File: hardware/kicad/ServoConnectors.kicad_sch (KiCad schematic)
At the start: 3 parts

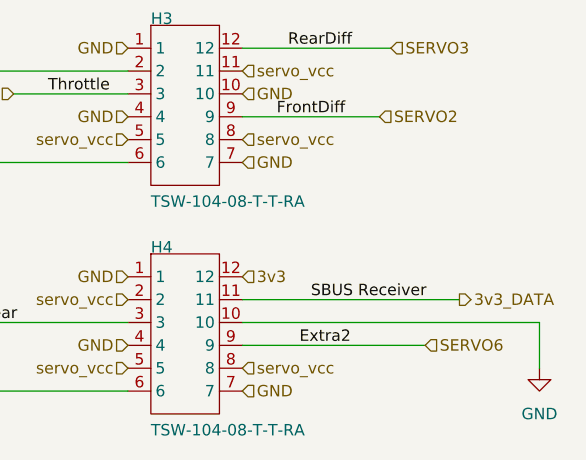
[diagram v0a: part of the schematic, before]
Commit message: servo buck and diode done, about to change order so highest current servos are closer to buck output
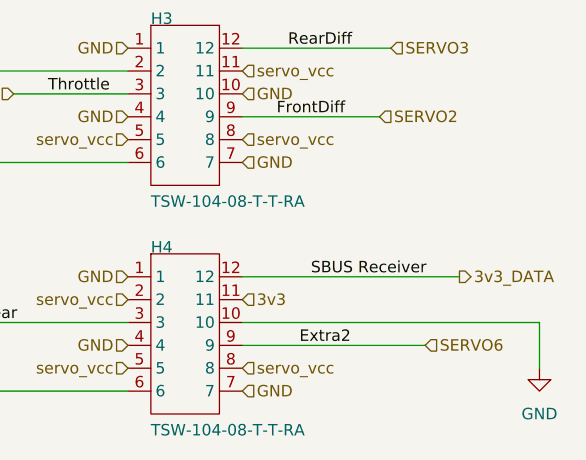
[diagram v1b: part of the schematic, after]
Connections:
- net 3v3: now also H4.11; no longer H4.12
- net 3v3_DATA: now also H4.12; no longer H4.11
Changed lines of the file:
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@@
-	(wire
-		(pts
-			(xy 187.96 106.68) (xy 163.83 106.68)
-		)
-		(stroke
-			(width 0)
-			(type default)
-		)
-	)
 	(wire
 		(pts
@@
 		(pts
 			(xy 196.85 109.22) (xy 196.85 114.3)
+		)
+		(stroke
+			(width 0)
+			(type default)
+		)
+	)
+	(wire
+		(pts
+			(xy 187.96 104.14) (xy 163.83 104.14)
 		)
 		(stroke
@@
 		)
 	)
+	(label "SBUS Receiver"
+		(at 171.45 104.14 0)
+		(effects
+			(font
+				(size 1.27 1.27)
+			)
+			(justify left bottom)
+		)
+	)
 	(label "RearDiff"
 		(at 168.91 78.74 0)
@@
 		)
 	)
-	(label "SBUS Receiver"
-		(at 171.45 106.68 0)
-		(effects
-			(font
-				(size 1.27 1.27)
-			)
-			(justify left bottom)
-		)
-	)
 	(hierarchical_label "THROTTLE_DATA_(SERVO_0)"
 		(shape input)
@@
 			)
 			(justify left)
-		)
-	)
-	(hierarchical_label "SERVO1"
-		(shape input)
-		(at 127 91.44 180)
-		(effects
-			(font
-				(size 1.27 1.27)
-			)
-			(justify right)
-		)
-	)
-	(hierarchical_label "GND"
-		(shape input)
-		(at 151.13 86.36 180)
-		(effects
-			(font
-				(size 1.27 1.27)
-			)
-			(justify right)
-		)
-	)
-	(hierarchical_label "GND"
-		(shape input)
-		(at 163.83 116.84 0)
-		(effects
-			(font
-				(size 1.27 1.27)
-			)
-			(justify left)
-		)
-	)
-	(hierarchical_label "servo_vcc"
-		(shape input)
-		(at 151.13 88.9 180)
-		(effects
-			(font
-				(size 1.27 1.27)
-			)
-			(justify right)
 		)
 	)
 	(hierarchical_label "3v3_DATA"
 		(shape output)
-		(at 187.96 106.68 0)
+		(at 187.96 104.14 0)
+		(effects
+			(font
+				(size 1.27 1.27)
+			)
+			(justify left)
+		)
+	)
+	(hierarchical_label "SERVO1"
+		(shape input)
+		(at 127 91.44 180)
+		(effects
+			(font
+				(size 1.27 1.27)
+			)
+			(justify right)
+		)
+	)
+	(hierarchical_label "GND"
+		(shape input)
+		(at 151.13 86.36 180)
+		(effects
+			(font
+				(size 1.27 1.27)
+			)
+			(justify right)
+		)
+	)
+	(hierarchical_label "GND"
+		(shape input)
+		(at 163.83 116.84 0)
+		(effects
+			(font
+				(size 1.27 1.27)
+			)
+			(justify left)
+		)
+	)
+	(hierarchical_label "servo_vcc"
+		(shape input)
+		(at 151.13 88.9 180)
+		(effects
+			(font
+				(size 1.27 1.27)
+			)
+			(justify right)
+		)
+	)
+	(hierarchical_label "3v3"
+		(shape input)
+		(at 163.83 106.68 0)
 		(effects
 			(font
@@
 		)
 	)
-	(hierarchical_label "3v3"
-		(shape input)
-		(at 163.83 104.14 0)
-		(effects
-			(font
-				(size 1.27 1.27)
-			)
-			(justify left)
-		)
-	)

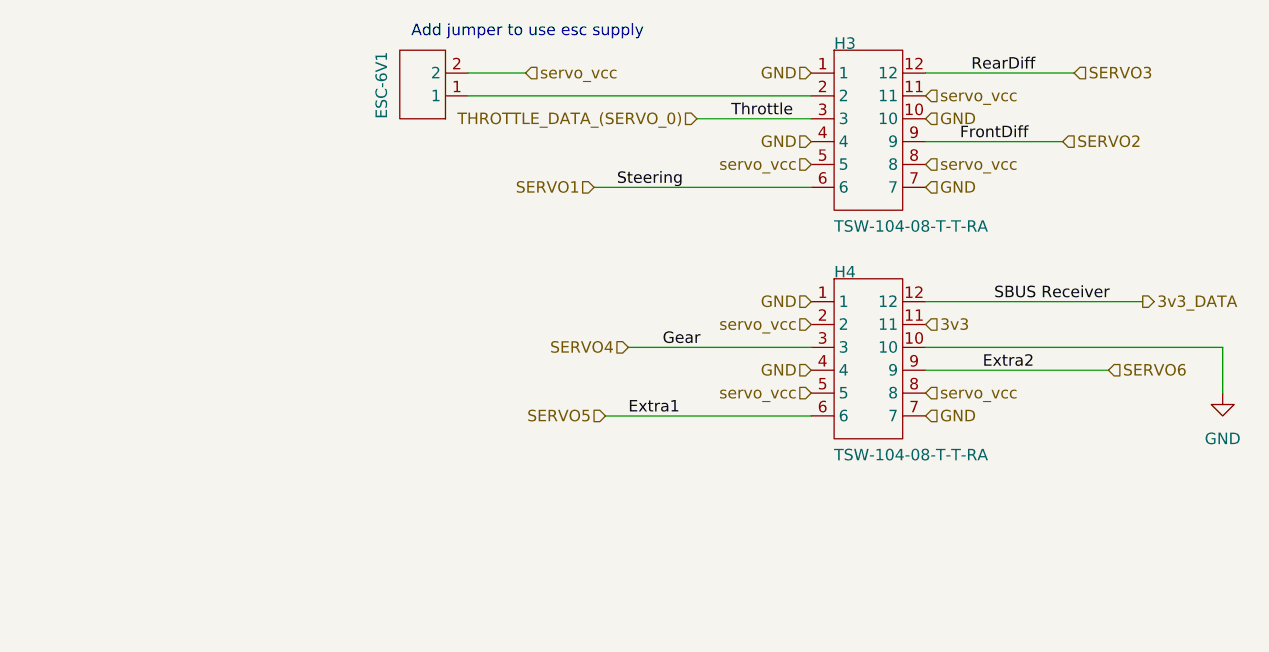
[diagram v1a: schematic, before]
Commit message: servo current sensor also done
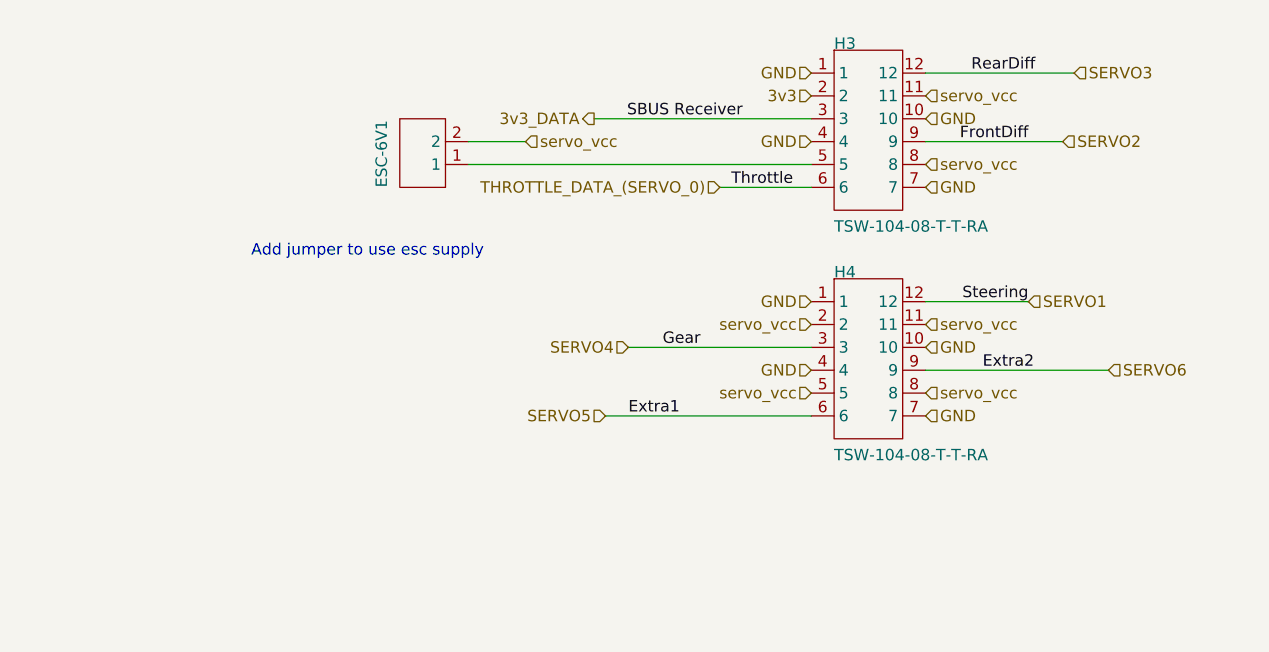
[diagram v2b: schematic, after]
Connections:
- net 3v3: now also H3.2; no longer H4.11
- net 3v3_DATA: now also H3.3; no longer H4.12
- net SERVO1: now also H4.12; no longer H3.6
- net THROTTLE_DATA_(SERVO_0): now also H3.6; no longer H3.3
- net servo_vcc: now also H4.11; no longer H3.5
- net at ESC-6V1.1: now also H3.5; no longer H3.2
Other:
- moved on the sheet: ESC-6V1

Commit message: new led connector
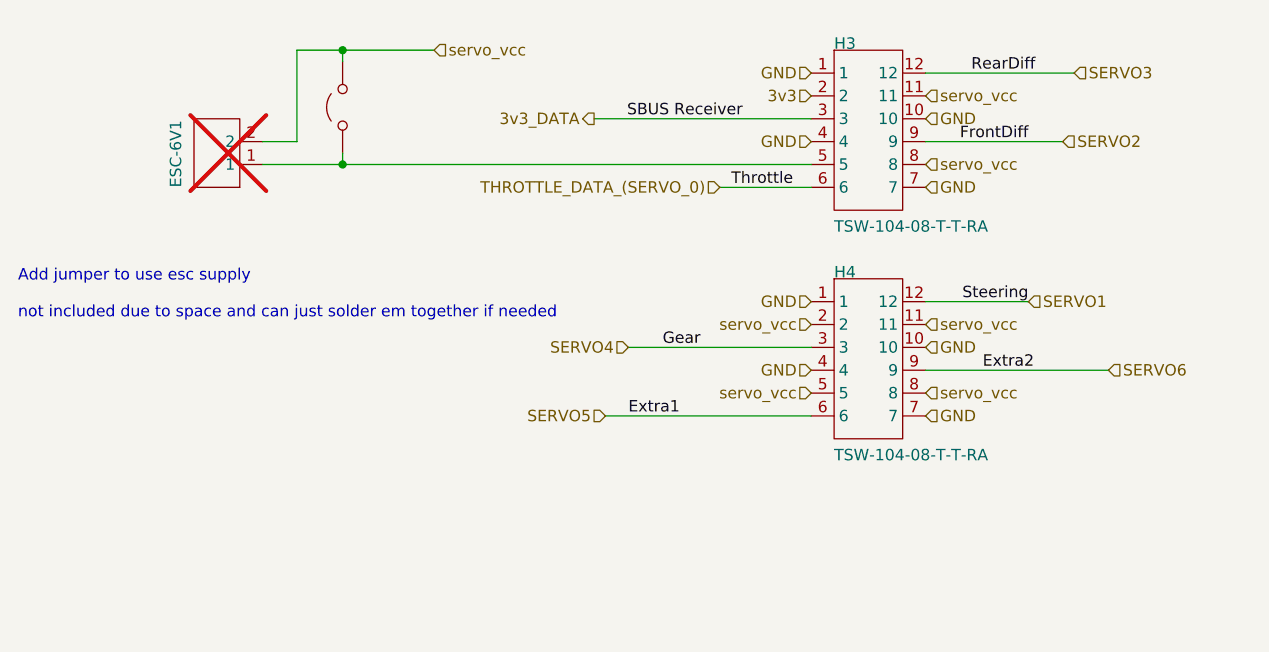
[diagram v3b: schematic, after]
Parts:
- added JP2101: Jumper_2_Open, PCM_SparkFun-Jumper:Jumper_2_NO, symbol Jumper:Jumper_2_Open
- ESC-6V1: now not fitted; now left out of the parts list
- H3: port11 (none) -> Rdiff; port2 (none) -> sbus; port5 (none) -> throttle; port8 (none) -> Fdiff
- H4: port11 (none) -> steer; port2 (none) -> gear; port5 (none) -> xtr1; port8 (none) -> xtr2
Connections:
- net servo_vcc: now also JP2101.2 (B)
- net at ESC-6V1.1, H3.5: now also JP2101.1 (A)
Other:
- note added: "Add jumper to use esc supply not included due to space and can just solder em together if needed"
- note removed: "Add jumper to use esc supply"
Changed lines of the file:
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@@
 	(generator_version "9.0")
 	(paper "A4")
-	(text "Add jumper to use esc supply"
+	(text "Add jumper to use esc supply\n\nnot included due to space and can just solder em together if needed"
 		(exclude_from_sim no)
-		(at 88.9 99.314 0)
+		(at 62.992 106.172 0)
 		(effects
 			(font
@@
 		)
 	)
-	(wire
-		(pts
-			(xy 113.03 86.36) (xy 119.38 86.36)
+	(junction
+		(at 99.06 88.9)
+		(diameter 0)
+		(color 0 0 0 0)
+	)
+	(junction
+		(at 99.06 76.2)
+		(diameter 0)
+		(color 0 0 0 0)
+	)
+	(wire
+		(pts
+			(xy 93.98 76.2) (xy 99.06 76.2)
+		)
+		(stroke
+			(width 0)
+			(type default)
+		)
+	)
+	(wire
+		(pts
+			(xy 93.98 86.36) (xy 90.17 86.36)
+		)
+		(stroke
+			(width 0)
+			(type default)
+		)
+	)
+	(wire
+		(pts
+			(xy 99.06 88.9) (xy 151.13 88.9)
 		)
 		(stroke
@@
 	(wire
 		(pts
+			(xy 99.06 87.63) (xy 99.06 88.9)
+		)
+		(stroke
+			(width 0)
+			(type default)
+		)
+	)
+	(wire
+		(pts
+			(xy 99.06 76.2) (xy 109.22 76.2)
+		)
+		(stroke
+			(width 0)
+			(type default)
+		)
+	)
+	(wire
+		(pts
 			(xy 180.34 78.74) (xy 163.83 78.74)
 		)
@@
 	(wire
 		(pts
-			(xy 113.03 88.9) (xy 151.13 88.9)
+			(xy 90.17 88.9) (xy 99.06 88.9)
 		)
 		(stroke
@@
 	(wire
 		(pts
+			(xy 99.06 76.2) (xy 99.06 77.47)
+		)
+		(stroke
+			(width 0)
+			(type default)
+		)
+	)
+	(wire
+		(pts
 			(xy 179.07 86.36) (xy 163.83 86.36)
+		)
+		(stroke
+			(width 0)
+			(type default)
+		)
+	)
+	(wire
+		(pts
+			(xy 93.98 76.2) (xy 93.98 86.36)
 		)
 		(stroke
@@
 	(hierarchical_label "servo_vcc"
 		(shape input)
-		(at 119.38 86.36 0)
+		(at 109.22 76.2 0)
 		(effects
 			(font
@@
 			)
 			(justify left)
+		)
+	)
+	(symbol
+		(lib_id "Jumper:Jumper_2_Open")
+		(at 99.06 82.55 90)
+		(unit 1)
+		(exclude_from_sim no)
+		(in_bom yes)
+		(on_board yes)
+		(dnp no)
+		(fields_autoplaced yes)
+		(property "Reference" "JP2101"
+			(at 100.33 81.2799 90)
+			(effects
+				(font
+					(size 1.27 1.27)
+				)
+				(justify right)
+				(hide yes)
+			)
+		)
+		(property "Value" "Jumper_2_Open"
+			(at 100.33 83.8199 90)
+			(effects
+				(font
+					(size 1.27 1.27)
+				)
+				(justify right)
+				(hide yes)
+			)
+		)
+		(property "Footprint" "PCM_SparkFun-Jumper:Jumper_2_NO"
+			(at 99.06 82.55 0)
+			(effects
+				(font
+					(size 1.27 1.27)
+				)
+				(hide yes)
+			)
+		)
+		(property "Datasheet" "~"
+			(at 99.06 82.55 0)
+			(effects
+				(font
+					(size 1.27 1.27)
+				)
+				(hide yes)
+			)
+		)
+		(property "Description" "Jumper, 2-pole, open"
+			(at 99.06 82.55 0)
+			(effects
+				(font
+					(size 1.27 1.27)
+				)
+				(hide yes)
+			)
+		)
+		(pin "1"
+		)
+		(pin "2"
+		)
+		(instances
+			(project ""
+				(path "/3f85abf4-0b95-4c4a-b7e9-06f59ca1ea3d/5c2e021f-c2d4-49e2-8c36-9a64f1f12001/e0f45e16-4740-446f-ae55-03461fa88791"
+					(reference "JP2101")
+					(unit 1)
+				)
+			)
 		)
 	)
@@
 			)
 		)
+		(property "port2" "sbus"
+			(at 157.48 85.09 0)
+			(effects
+				(font
+					(size 1.27 1.27)
+				)
+				(hide yes)
+			)
+		)
+		(property "port5" "throttle"
+			(at 157.48 85.09 0)
+			(effects
+				(font
+					(size 1.27 1.27)
+				)
+				(hide yes)
+			)
+		)
+		(property "port8" "Fdiff"
+			(at 157.48 85.09 0)
+			(effects
+				(font
+					(size 1.27 1.27)
+				)
+				(hide yes)
+			)
+		)
+		(property "port11" "Rdiff"
+			(at 157.48 85.09 0)
+			(effects
+				(font
+					(size 1.27 1.27)
+				)
+				(hide yes)
+			)
+		)
 		(pin "1"
 		)
@@
 			)
 		)
+		(property "port2" "gear"
+			(at 157.48 110.49 0)
+			(effects
+				(font
+					(size 1.27 1.27)
+				)
+				(hide yes)
+			)
+		)
+		(property "port5" "xtr1"
+			(at 157.48 110.49 0)
+			(effects
+				(font
+					(size 1.27 1.27)
+				)
+				(hide yes)
+			)
+		)
+		(property "port8" "xtr2"
+			(at 157.48 110.49 0)
+			(effects
+				(font
+					(size 1.27 1.27)
+				)
+				(hide yes)
+			)
+		)
+		(property "port11" "steer"
+			(at 157.48 110.49 0)
+			(effects
+				(font
+					(size 1.27 1.27)
+				)
+				(hide yes)
+			)
+		)
 		(pin "4"
 		)
@@
 	(symbol
 		(lib_id "5v rail sm-easyedapro:PZ254V-11-02P")
-		(at 107.95 87.63 180)
+		(at 85.09 87.63 180)
 		(unit 1)
 		(exclude_from_sim no)
-		(in_bom yes)
-		(on_board yes)
-		(dnp no)
+		(in_bom no)
+		(on_board no)
+		(dnp yes)
 		(property "Reference" "ESC-6V1"
-			(at 104.14 91.44 90)
+			(at 81.28 91.44 90)
 			(effects
 				(font
@@
 		)
 		(property "Value" "PZ254V-11-02P"
-			(at 105.41 93.98 0)
+			(at 82.55 93.98 0)
 			(effects
 				(font
@@
 		)
 		(property "Footprint" "Connector_PinHeader_2.54mm:PinHeader_1x02_P2.54mm_Vertical"
-			(at 107.95 87.63 0)
+			(at 85.09 87.63 0)
 			(effects
 				(font
@@
 		)
 		(property "Datasheet" "https://item.szlcsc.com/datasheet/PZ254V-11-02P/502957.html"
-			(at 107.95 87.63 0)
+			(at 85.09 87.63 0)
 			(effects
 				(font
@@
 		)
 		(property "Description" "Pin Structure:1x2P Pitch:2.54mm Row Spacing:- Circluar Pins/Square Pins:Pin Header Mounting Type:Through Hole Number of Rows:1 Number of Pins:2P Current Rating:- Voltage Rating (Max):- Length of Mating Pin:6mm Insulation Height:2.5mm Length of End Connect"
-			(at 107.95 87.63 0)
+			(at 85.09 87.63 0)
 			(effects
 				(font
@@
 		)
 		(property "Manufacturer Part" "PZ254V-11-02P"
-			(at 107.95 87.63 0)
+			(at 85.09 87.63 0)
 			(effects
 				(font
@@
 		)
 		(property "Manufacturer" "XFCN(兴飞)"
-			(at 107.95 87.63 0)
+			(at 85.09 87.63 0)
 			(effects
 				(font
@@
 		)
 		(property "Supplier Part" "C492401"
-			(at 107.95 87.63 0)
+			(at 85.09 87.63 0)
 			(effects
 				(font
@@
 		)
 		(property "Supplier" "LCSC"
-			(at 107.95 87.63 0)
+			(at 85.09 87.63 0)
 			(effects
 				(font
@@
 		)
 		(property "LCSC Part Name" "1x2P 间距:2.54mm 方针 直插"
-			(at 107.95 87.63 0)
-			(effects
-				(font
+			(at 85.09 87.63 0)
+			(effects
+				(font

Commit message: starting erc check
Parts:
- ESC-6V1: footprint Connector_PinHeader_2.54mm:PinHeader_1x02_P2.54mm_Vertical -> 5v rail sm-easyedapro:HDR-TH_2P-P2.54-V-M
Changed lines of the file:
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@@
 			)
 		)
-		(property "Footprint" "Connector_PinHeader_2.54mm:PinHeader_1x02_P2.54mm_Vertical"
+		(property "Footprint" "5v rail sm-easyedapro:HDR-TH_2P-P2.54-V-M"
 			(at 85.09 87.63 0)
 			(effects

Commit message: Update KiCad footprints and schematic placements
Convert and normalize multiple KiCad footprints and adjust schematic symbol placements. Upgraded EasyEDA and JLCImport footprints to modern pcbnew/footprint format (updated fp_line/pad primitives, uuids, embedded fonts/models), adjusted 3D model offsets, and expanded pad metadata. In schematics: moved EXB2HV102JV symbol position and added mirror Y, removed fields_autoplaced, set instance project path for U3201, and updated ServoConnectors port2 label to "sbus 3V". Also refreshed various PCB fp element UUIDs in svea_powerboard_rev3.kicad_pcb.
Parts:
- H3: port2 sbus -> sbus 3V
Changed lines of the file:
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@@
 			)
 		)
-		(property "port2" "sbus"
+		(property "port2" "sbus 3V"
 			(at 157.48 85.09 0)
 			(effects

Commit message: updated more footprints
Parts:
- JP2101: footprint PCM_SparkFun-Jumper:Jumper_2_NO -> Jumper:SolderJumper-2_P1.3mm_Open_TrianglePad1.0x1.5mm
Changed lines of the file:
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@@
 			)
 		)
-		(property "Footprint" "PCM_SparkFun-Jumper:Jumper_2_NO"
+		(property "Footprint" "Jumper:SolderJumper-2_P1.3mm_Open_TrianglePad1.0x1.5mm"
 			(at 99.06 82.55 0)
 			(effects

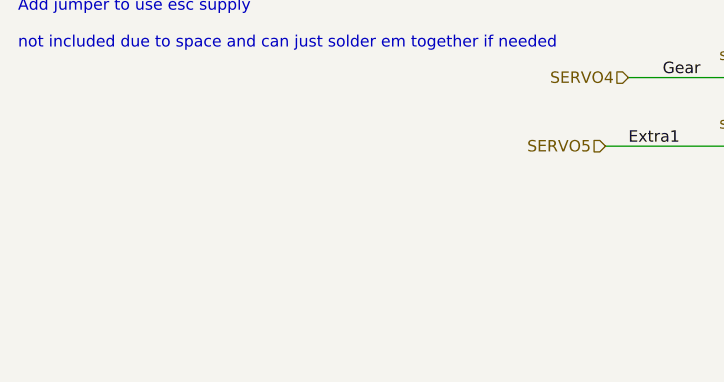
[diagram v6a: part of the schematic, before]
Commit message: starting erc check
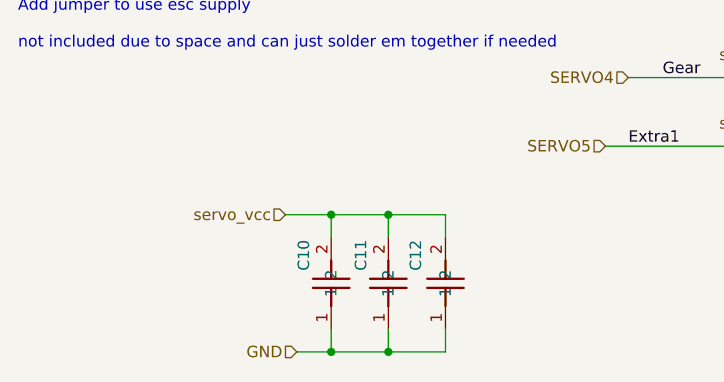
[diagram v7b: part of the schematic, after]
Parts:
- added C10, C11, C12: HGC1206R5107M100NSPJ, JLCImport:HGC1206R5107M100NSPJ, symbol JLCImport:HGC1206R5107M100NSPJ
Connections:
- net GND: now also C10.1, C11.1, C12.1
- net servo_vcc: now also C10.2, C11.2, C12.2

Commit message: update
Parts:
- added C2101: HGC1206R5107M100NSPJ, JLCImport:HGC1206R5107M100NSPJ, symbol JLCImport:HGC1206R5107M100NSPJ
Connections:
- net GND: now also C2101.1
- net servo_vcc: now also C2101.2
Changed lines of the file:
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@@
+	)
+	(junction
+		(at 110.49 139.7)
+		(diameter 0)
+		(color 0 0 0 0)
+	)
+	(junction
+		(at 110.49 124.46)
+		(diameter 0)
+		(color 0 0 0 0)
 	)
 	(junction
@@
 	)
 	(junction
+		(at 116.84 139.7)
+		(diameter 0)
+		(color 0 0 0 0)
+	)
+	(junction
+		(at 116.84 124.46)
+		(diameter 0)
+		(color 0 0 0 0)
+	)
+	(junction
 		(at 97.79 139.7)
 		(diameter 0)
@@
 	(wire
 		(pts
+			(xy 110.49 124.46) (xy 116.84 124.46)
+		)
+		(stroke
+			(width 0)
+			(type default)
+		)
+	)
+	(wire
+		(pts
 			(xy 97.79 139.7) (xy 104.14 139.7)
 		)
@@
 	(wire
 		(pts
+			(xy 110.49 139.7) (xy 116.84 139.7)
+		)
+		(stroke
+			(width 0)
+			(type default)
+		)
+	)
+	(wire
+		(pts
 			(xy 99.06 88.9) (xy 151.13 88.9)
 		)
@@
 	(wire
 		(pts
+			(xy 124.46 137.16) (xy 124.46 139.7)
+		)
+		(stroke
+			(width 0)
+			(type default)
+		)
+	)
+	(wire
+		(pts
 			(xy 184.15 111.76) (xy 163.83 111.76)
 		)
@@
 	(wire
 		(pts
-			(xy 110.49 139.7) (xy 104.14 139.7)
+			(xy 104.14 139.7) (xy 110.49 139.7)
 		)
 		(stroke
@@
 	(wire
 		(pts
+			(xy 116.84 127) (xy 116.84 124.46)
+		)
+		(stroke
+			(width 0)
+			(type default)
+		)
+	)
+	(wire
+		(pts
+			(xy 116.84 137.16) (xy 116.84 139.7)
+		)
+		(stroke
+			(width 0)
+			(type default)
+		)
+	)
+	(wire
+		(pts
 			(xy 110.49 127) (xy 110.49 124.46)
 		)
@@
 	(wire
 		(pts
+			(xy 116.84 124.46) (xy 124.46 124.46)
+		)
+		(stroke
+			(width 0)
+			(type default)
+		)
+	)
+	(wire
+		(pts
 			(xy 175.26 104.14) (xy 163.83 104.14)
 		)
@@
 	(wire
 		(pts
+			(xy 124.46 127) (xy 124.46 124.46)
+		)
+		(stroke
+			(width 0)
+			(type default)
+		)
+	)
+	(wire
+		(pts
 			(xy 92.71 124.46) (xy 97.79 124.46)
 		)
@@
 	(wire
 		(pts
+			(xy 116.84 139.7) (xy 124.46 139.7)
+		)
+		(stroke
+			(width 0)
+			(type default)
+		)
+	)
+	(wire
+		(pts
 			(xy 179.07 86.36) (xy 163.83 86.36)
 		)
@@
 	(wire
 		(pts
-			(xy 110.49 124.46) (xy 104.14 124.46)
+			(xy 104.14 124.46) (xy 110.49 124.46)
 		)
 		(stroke
@@
 					(unit 1)
 				)
+			)
+		)
+	)
+	(symbol
+		(lib_id "JLCImport:HGC1206R5107M100NSPJ")
+		(at 116.84 132.08 90)
+		(unit 1)
+		(exclude_from_sim no)
+		(in_bom yes)
+		(on_board yes)
+		(dnp no)
+		(property "Reference" "C2101"
+			(at 113.538 127.254 0)
+			(effects
+				(font
+					(size 1.27 1.27)
+				)
+				(justify right)
+			)
+		)
+		(property "Value" "HGC1206R5107M100NSPJ"
+			(at 120.65 133.3499 90)
+			(effects
+				(font
+					(size 1.27 1.27)
+				)
+				(justify right)
+				(hide yes)
+			)
+		)
+		(property "Footprint" "JLCImport:HGC1206R5107M100NSPJ"
+			(at 116.84 132.08 0)
+			(effects
+				(font
+					(size 1.27 1.27)
+				)
+				(hide yes)
+			)
+		)
+		(property "Datasheet" "https://item.szlcsc.com/89171.html"
+			(at 116.84 132.08 0)
+			(effects
+				(font
+					(size 1.27 1.27)
+				)
+				(hide yes)
+			)
+		)
+		(property "Description" "100uF ±20% 10V Ceramic Capacitor X5R 1206"
+			(at 116.84 132.08 0)
+			(effects
+				(font
+					(size 1.27 1.27)
+				)
+				(hide yes)
+			)
+		)
+		(property "LCSC" "C7432784"
+			(at 116.84 132.08 0)
+			(effects
+				(font
+					(size 1.27 1.27)
+				)
+				(hide yes)
+			)
+		)
+		(property "Manufacturer" "Chinocera(华瓷)"
+			(at 116.84 132.08 0)
+			(effects
+				(font
+					(size 1.27 1.27)
+				)
+				(hide yes)
+			)
+		)
+		(property "Manufacturer Part" "HGC1206R5107M100NSPJ"
+			(at 116.84 132.08 0)
+			(effects
+				(font
+					(size 1.27 1.27)
+				)
+				(hide yes)
+			)
+		)
+		(property "Des" ""
+			(at 116.84 132.08 90)
+			(effects
+				(font
+					(size 1.27 1.27)
+				)
+				(hide yes)
+			)
+		)
+		(pin "1"
+		)
+		(pin "2"
+		)
+		(instances
+			(project "svea_powerboard_rev3"
+				(path "/3f85abf4-0b95-4c4a-b7e9-06f59ca1ea3d/5c2e021f-c2d4-49e2-8c36-9a64f1f12001/e0f45e16-4740-446f-ae55-03461fa88791"
+					(reference "C2101")
+					(unit 1)
+				)
